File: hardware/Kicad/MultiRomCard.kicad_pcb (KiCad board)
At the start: 2 copper layers, 160 x 100 mm, 17 parts, among them P1 VC4000_Cartridge_Bus, P2 MicroSD_Breakout, U1 Arduino_Nano, U2 74HC595, U3 74HC595, U4 74HC595, U5 6264, U6 74HC245, U7 74HC245, U8 74HC245

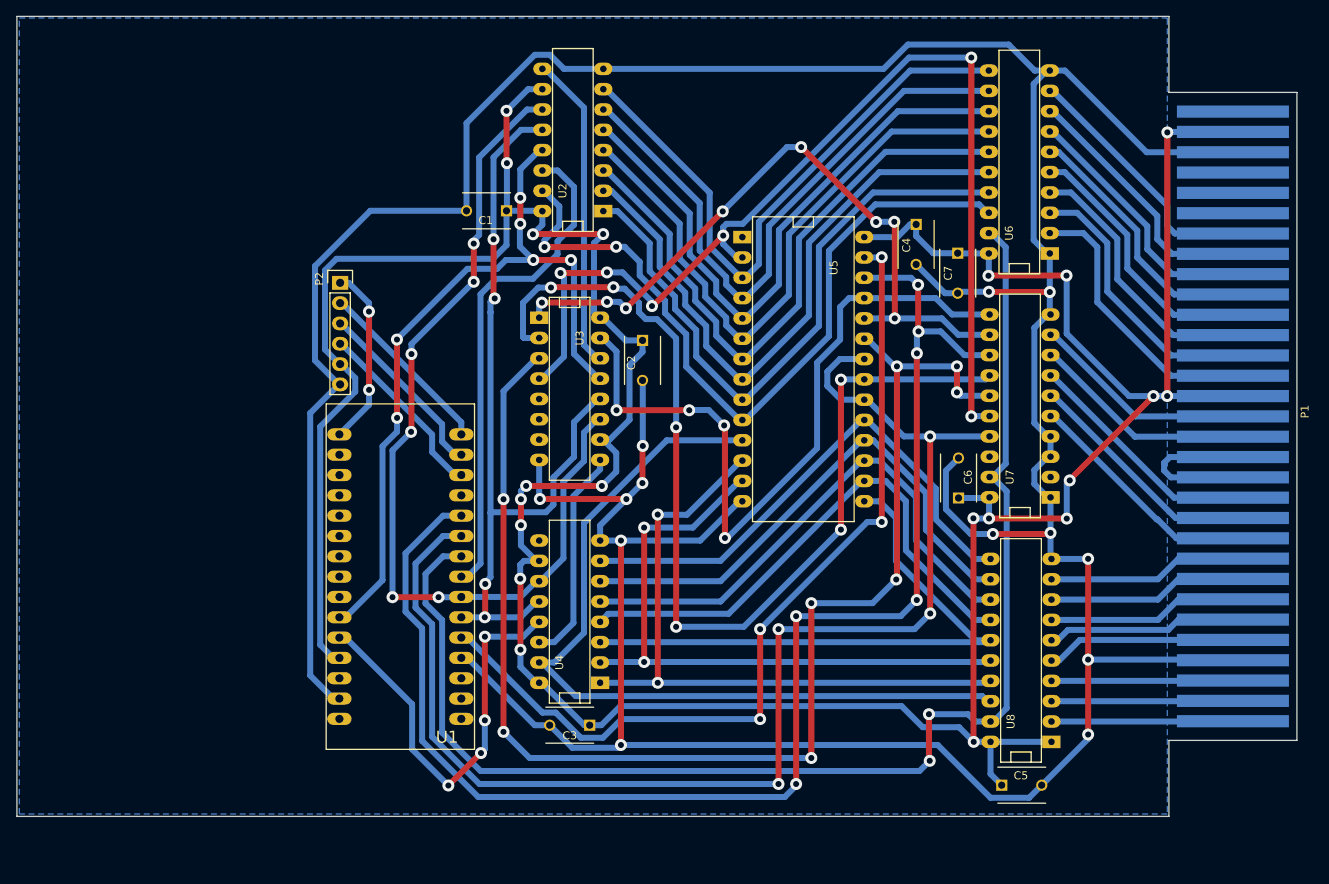
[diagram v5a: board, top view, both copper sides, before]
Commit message: [PCB] Some minor routing improvements.
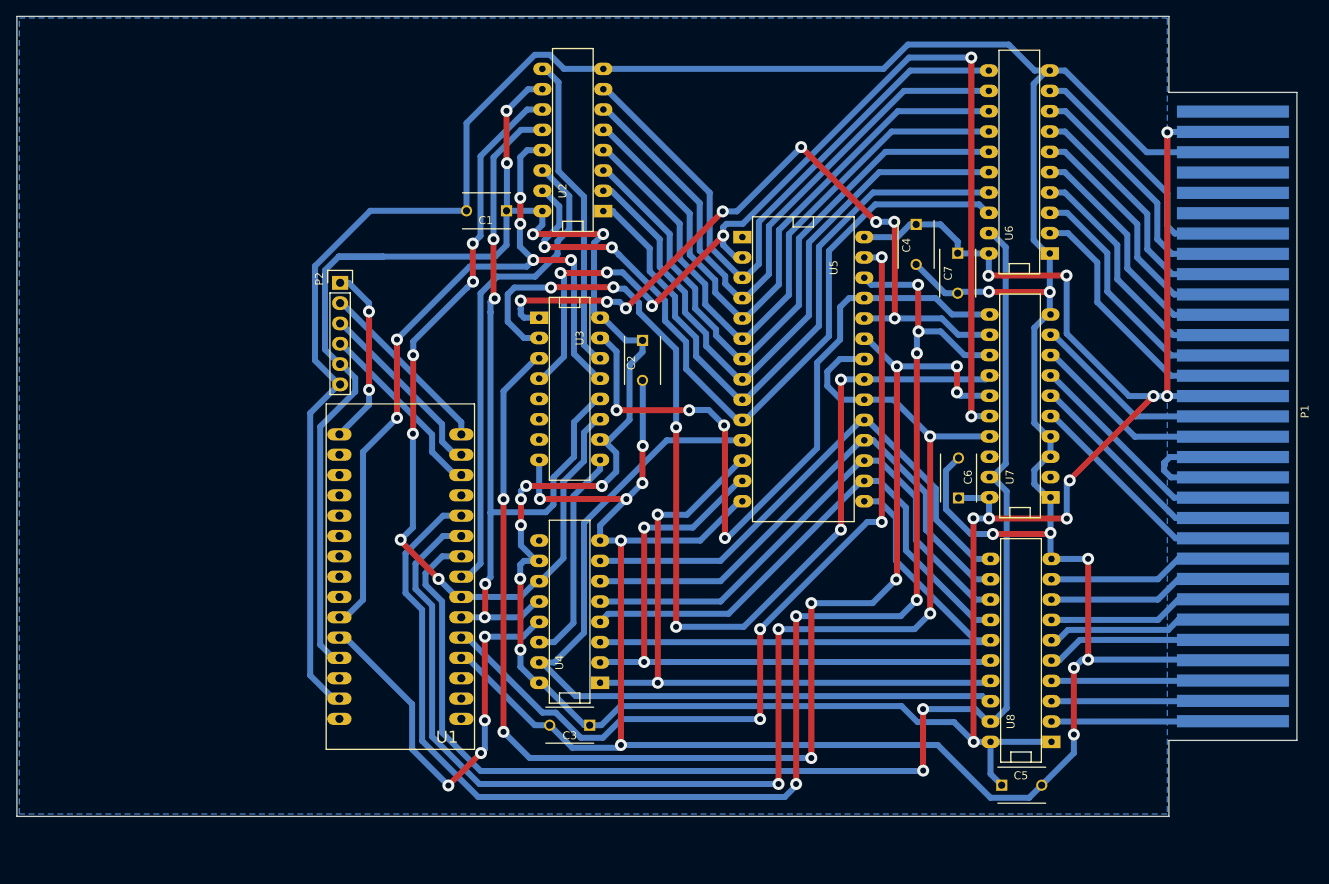
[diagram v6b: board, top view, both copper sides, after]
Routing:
- net VCC: track 440.6 -> 446.2 mm
- net Net-(U1-Pad7): track 112.7 -> 107.2 mm
- net /A9: track 87.5 -> 92.3 mm
- net /A10: track 129.4 -> 132.0 mm
- net Net-(U1-Pad8): track 62.5 -> 61.1 mm
- net OEVCBUS: track 168.6 -> 170.0 mm
- net /EA0: track 34.3 -> 33.2 mm
- net /EA6: track 32.0 -> 32.9 mm
- net /EA7: track 31.8 -> 32.7 mm
- net /EA5: track 32.0 -> 32.9 mm
- net Net-(U1-Pad25): track 96.3 -> 97.2 mm
- net /A0: track 95.4 -> 94.6 mm
- net /EA1: track 33.8 -> 33.1 mm
- net GND: track 524.4 -> 524.8 mm, vias 13 -> 14

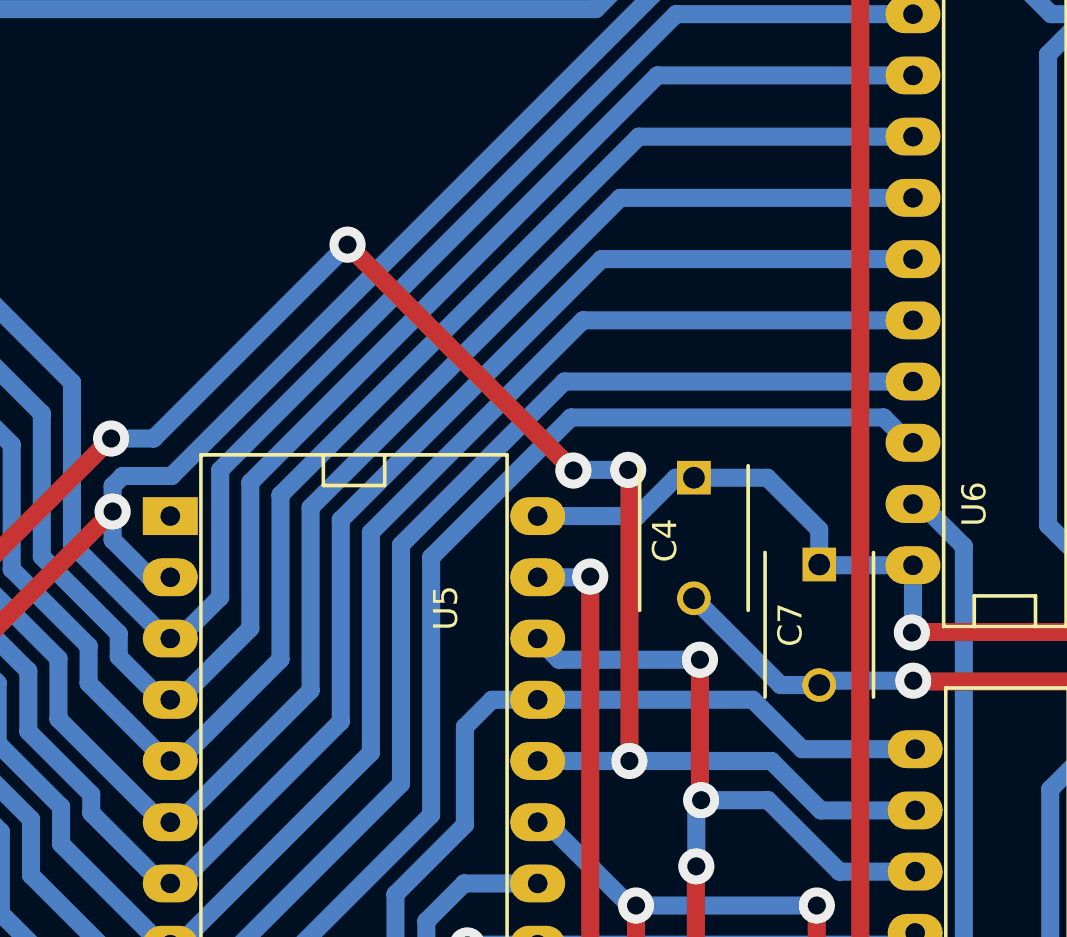
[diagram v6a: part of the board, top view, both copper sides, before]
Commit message: [PCB] Increase one inner GND zone a little.
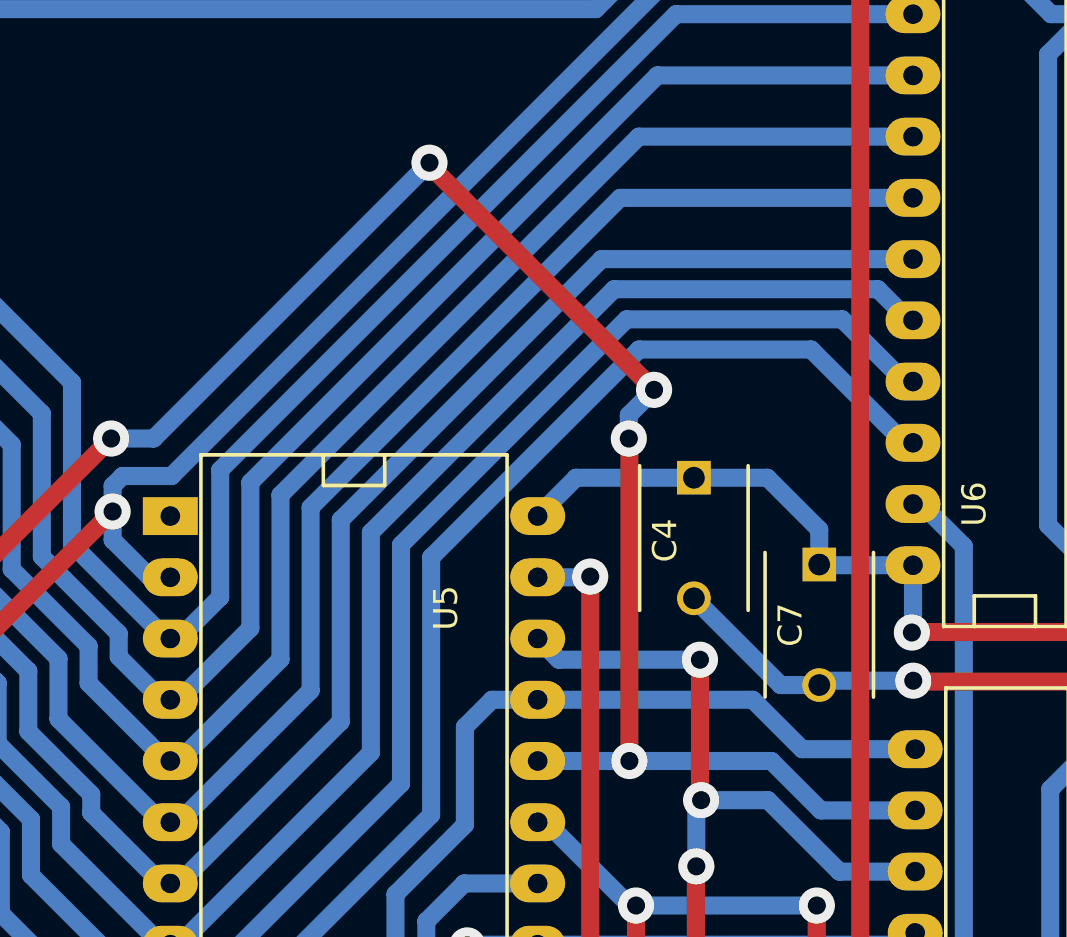
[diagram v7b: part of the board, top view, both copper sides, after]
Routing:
- net /A9: track 92.3 -> 98.6 mm
- net /A0: track 94.6 -> 96.9 mm
- net /A1: track 79.0 -> 81.2 mm
- net /A2: track 78.5 -> 79.5 mm
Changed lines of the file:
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@@
     (thickness 1.6)
     (drawings 8)
-    (tracks 916)
+    (tracks 920)
     (zones 0)
     (modules 17)
@@
   (title_block
     (title "Interton VC4000 MultiRom Cartridge")
-    (date "Tuesday, June 23, 2015")
+    (date "Thursday, June 25, 2015")
     (rev 0.1)
     (company "Mario Keller and Johannes Maibaum")
@@
   (segment (start 174.570055 65.43) (end 187.49 65.43) (width 0.75) (layer B.Cu) (net 9) (status 20))
   (segment (start 163.74997 76.250085) (end 174.570055 65.43) (width 0.75) (layer B.Cu) (net 9))
+  (segment (start 156.68 93.87) (end 157.0356 93.87) (width 0.75) (layer B.Cu) (net 10))
+  (segment (start 157.0356 93.87) (end 164.99998 85.90562) (width 0.75) (layer B.Cu) (net 10))
+  (segment (start 164.99998 85.90562) (end 164.99998 76.767856) (width 0.75) (layer B.Cu) (net 10))
+  (segment (start 164.99998 76.767856) (end 175.087825 66.68001) (width 0.75) (layer B.Cu) (net 10))
+  (segment (start 175.087825 66.68001) (end 186.033408 66.68001) (width 0.75) (layer B.Cu) (net 10))
+  (segment (start 186.033408 66.68001) (end 187.323398 67.97) (width 0.75) (layer B.Cu) (net 10))
+  (segment (start 187.323398 67.97) (end 187.49 67.97) (width 0.75) (layer B.Cu) (net 10))
   (segment (start 156.68 93.87) (end 156.3244 93.87) (width 0.75) (layer B.Cu) (net 10) (status 30))
   (segment (start 140.3 70.3) (end 139.3 70.3) (width 0.75) (layer B.Cu) (net 10) (status 30))
@@
   (segment (start 146.34995 76.34995) (end 140.3 70.3) (width 0.75) (layer B.Cu) (net 10) (status 20))
   (segment (start 149.518368 83.013875) (end 146.34995 79.845457) (width 0.75) (layer B.Cu) (net 10))
-  (segment (start 156.68 93.87) (end 157.0356 93.87) (width 0.75) (layer B.Cu) (net 10) (status 30))
-  (segment (start 164.99998 76.767856) (end 173.797836 67.97) (width 0.75) (layer B.Cu) (net 10))
-  (segment (start 157.0356 93.87) (end 164.99998 85.90562) (width 0.75) (layer B.Cu) (net 10) (status 10))
-  (segment (start 164.99998 85.90562) (end 164.99998 76.767856) (width 0.75) (layer B.Cu) (net 10))
-  (segment (start 173.797836 67.97) (end 187.49 67.97) (width 0.75) (layer B.Cu) (net 10) (status 20))
+  (segment (start 156.68 96.41) (end 157.0356 96.41) (width 0.75) (layer B.Cu) (net 11))
+  (segment (start 157.0356 96.41) (end 166.24999 87.19561) (width 0.75) (layer B.Cu) (net 11))
+  (segment (start 166.24999 87.19561) (end 166.24999 77.285627) (width 0.75) (layer B.Cu) (net 11))
+  (segment (start 166.24999 77.285627) (end 175.605596 67.93002) (width 0.75) (layer B.Cu) (net 11))
+  (segment (start 175.605596 67.93002) (end 184.55442 67.93002) (width 0.75) (layer B.Cu) (net 11))
+  (segment (start 184.55442 67.93002) (end 187.1344 70.51) (width 0.75) (layer B.Cu) (net 11))
+  (segment (start 187.1344 70.51) (end 187.49 70.51) (width 0.75) (layer B.Cu) (net 11))
   (segment (start 156.68 96.41) (end 156.3244 96.41) (width 0.75) (layer B.Cu) (net 11) (status 30))
   (segment (start 156.3244 96.41) (end 150.90002 90.98562) (width 0.75) (layer B.Cu) (net 11) (status 10))
@@
   (segment (start 145.09994 77.488736) (end 140.494016 72.882812) (width 0.75) (layer B.Cu) (net 11))
   (segment (start 140.494016 72.882812) (end 140.494016 72.84) (width 0.75) (layer B.Cu) (net 11))
-  (segment (start 166.24999 77.285627) (end 166.24999 87.19561) (width 0.75) (layer B.Cu) (net 11))
-  (segment (start 156.68 96.41) (end 157.0356 96.41) (width 0.75) (layer B.Cu) (net 11) (status 30))
-  (segment (start 157.0356 96.41) (end 166.24999 87.19561) (width 0.75) (layer B.Cu) (net 11) (status 10))
-  (segment (start 166.24999 77.285627) (end 173.025617 70.51) (width 0.75) (layer B.Cu) (net 11))
-  (segment (start 173.025617 70.51) (end 187.49 70.51) (width 0.75) (layer B.Cu) (net 11) (status 20))
+  (segment (start 156.68 98.95) (end 157.0356 98.95) (width 0.75) (layer B.Cu) (net 12))
+  (segment (start 157.0356 98.95) (end 167.5 88.4856) (width 0.75) (layer B.Cu) (net 12))
+  (segment (start 167.5 88.4856) (end 167.5 77.803398) (width 0.75) (layer B.Cu) (net 12))
+  (segment (start 183.26443 69.18003) (end 187.1344 73.05) (width 0.75) (layer B.Cu) (net 12))
+  (segment (start 167.5 77.803398) (end 176.123366 69.18003) (width 0.75) (layer B.Cu) (net 12))
+  (segment (start 187.1344 73.05) (end 187.49 73.05) (width 0.75) (layer B.Cu) (net 12))
+  (segment (start 176.123366 69.18003) (end 183.26443 69.18003) (width 0.75) (layer B.Cu) (net 12))
   (segment (start 156.68 98.95) (end 156.028444 98.95) (width 0.75) (layer B.Cu) (net 12) (status 30))
   (segment (start 156.028444 98.95) (end 149.65001 92.571566) (width 0.75) (layer B.Cu) (net 12) (status 10))
@@
   (segment (start 133.8 72.253398) (end 131.846602 70.3) (width 0.75) (layer B.Cu) (net 12) (status 20))
   (segment (start 131.846602 70.3) (end 131.68 70.3) (width 0.75) (layer B.Cu) (net 12) (status 30))
-  (segment (start 156.68 98.95) (end 157.0356 98.95) (width 0.75) (layer B.Cu) (net 12) (status 30))
-  (segment (start 157.0356 98.95) (end 167.5 88.4856) (width 0.75) (layer B.Cu) (net 12) (status 10))
-  (segment (start 167.5 88.4856) (end 167.5 77.803398) (width 0.75) (layer B.Cu) (net 12))
-  (segment (start 186.273398 72) (end 187.323398 73.05) (width 0.75) (layer B.Cu) (net 12) (status 20))
-  (segment (start 167.5 77.803398) (end 173.303398 72) (width 0.75) (layer B.Cu) (net 12))
-  (segment (start 173.303398 72) (end 186.273398 72) (width 0.75) (layer B.Cu) (net 12))
-  (segment (start 187.323398 73.05) (end 187.49 73.05) (width 0.75) (layer B.Cu) (net 12) (status 30))
+  (segment (start 178.4 74.5) (end 173.51 74.5) (width 0.75) (layer B.Cu) (net 13))
+  (segment (start 173.51 74.5) (end 171.92 76.09) (width 0.75) (layer B.Cu) (net 13))
   (segment (start 185.599872 139.18) (end 183.132284 136.712412) (width 0.75) (layer B.Cu) (net 13))
   (segment (start 183.132284 136.712412) (end 178.5824 136.712412) (width 0.75) (layer B.Cu) (net 13))
@@
   (segment (start 138.9 86.16) (end 138.76 86.16) (width 0.75) (layer B.Cu) (net 13) (status 30))
   (segment (start 138.76 86.16) (end 138.132 85.532) (width 0.75) (layer B.Cu) (net 13) (status 30))
-  (segment (start 178.4 74.5) (end 177.645966 74.5) (width 0.75) (layer B.Cu) (net 13) (status 10))
-  (segment (start 171.92 76.09) (end 176.055966 76.09) (width 0.75) (layer B.Cu) (net 13) (status 10))
-  (segment (start 176.055966 76.09) (end 177.645966 74.5) (width 0.75) (layer B.Cu) (net 13))
   (segment (start 144.2 89) (end 142.0956 89) (width 0.75) (layer B.Cu) (net 13) (status 10))
   (segment (start 142.0956 89) (end 139.2556 86.16) (width 0.75) (layer B.Cu) (net 13) (status 20))
@@
   (via (at 154.403443 99.628943) (size 1.5) (drill 0.75) (layers F.Cu B.Cu) (net 14))
   (via (at 154.5 113.7) (size 1.5) (drill 0.75) (layers F.Cu B.Cu) (net 14))
+  (segment (start 167.43152 61.43152) (end 155.989864 72.873176) (width 0.75) (layer B.Cu) (net 15))
+  (segment (start 176.748233 70.853273) (end 167.43152 61.53656) (width 0.75) (layer F.Cu) (net 15))
+  (segment (start 167.43152 61.53656) (end 167.43152 61.43152) (width 0.75) (layer F.Cu) (net 15))
+  (via (at 167.43152 61.43152) (size 1.5) (drill 0.75) (layers F.Cu B.Cu) (net 15))
+  (segment (start 175.7 72.87499) (end 175.7 71.901506) (width 0.75) (layer B.Cu) (net 15))
+  (segment (start 175.7 71.901506) (end 176.748233 70.853273) (width 0.75) (layer B.Cu) (net 15))
+  (via (at 176.748233 70.853273) (size 1.5) (drill 0.75) (layers F.Cu B.Cu) (net 15))
+  (segment (start 175.72501 86.25) (end 175.72501 72.9) (width 0.75) (layer F.Cu) (net 15))
+  (segment (start 175.72501 72.9) (end 175.7 72.87499) (width 0.75) (layer F.Cu) (net 15))
+  (via (at 175.7 72.87499) (size 1.5) (drill 0.75) (layers F.Cu B.Cu) (net 15))
   (segment (start 128.97866 85.087122) (end 128.97866 85.75166) (width 0.75) (layer B.Cu) (net 15))
   (segment (start 128.97866 85.75166) (end 129.387 86.16) (width 0.75) (layer B.Cu) (net 15))
@@
   (via (at 128.97183 84.019632) (size 1.5) (drill 0.75) (layers F.Cu B.Cu) (net 15))
   (segment (start 154.225004 72.873176) (end 155.989864 72.873176) (width 0.75) (layer B.Cu) (net 15))
-  (segment (start 155.989864 72.873176) (end 164.03152 64.83152) (width 0.75) (layer B.Cu) (net 15))
   (segment (start 154.225004 72.873176) (end 142.126379 84.971801) (width 0.75) (layer F.Cu) (net 15))
   (segment (start 142.126379 84.971801) (end 142.126379 84.991118) (width 0.75) (layer F.Cu) (net 15))
   (via (at 142.126379 84.991118) (size 1.5) (drill 0.75) (layers F.Cu B.Cu) (net 15))
   (via (at 154.225004 72.873176) (size 1.5) (drill 0.75) (layers F.Cu B.Cu) (net 15))
-  (segment (start 173.400754 74.200754) (end 164.03152 64.83152) (width 0.75) (layer F.Cu) (net 15))
-  (via (at 164.03152 64.83152) (size 1.5) (drill 0.75) (layers F.Cu B.Cu) (net 15))
-  (segment (start 175.673928 74.173928) (end 173.42758 74.173928) (width 0.75) (layer B.Cu) (net 15))
-  (segment (start 173.42758 74.173928) (end 173.400754 74.200754) (width 0.75) (layer B.Cu) (net 15))
-  (via (at 173.400754 74.200754) (size 1.5) (drill 0.75) (layers F.Cu B.Cu) (net 15))
-  (segment (start 175.72501 86.25) (end 175.72501 74.22501) (width 0.75) (layer F.Cu) (net 15))
-  (segment (start 175.72501 74.22501) (end 175.673928 74.173928) (width 0.75) (layer F.Cu) (net 15))
-  (via (at 175.673928 74.173928) (size 1.5) (drill 0.75) (layers F.Cu B.Cu) (net 15))
   (segment (start 175.565942 86.25) (end 181.614439 86.25) (width 0.75) (layer B.Cu) (net 15))
   (segment (start 171.92 86.25) (end 175.565942 86.25) (width 0.75) (layer B.Cu) (net 15) (status 10))
